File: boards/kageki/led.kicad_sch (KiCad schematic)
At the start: 50 parts

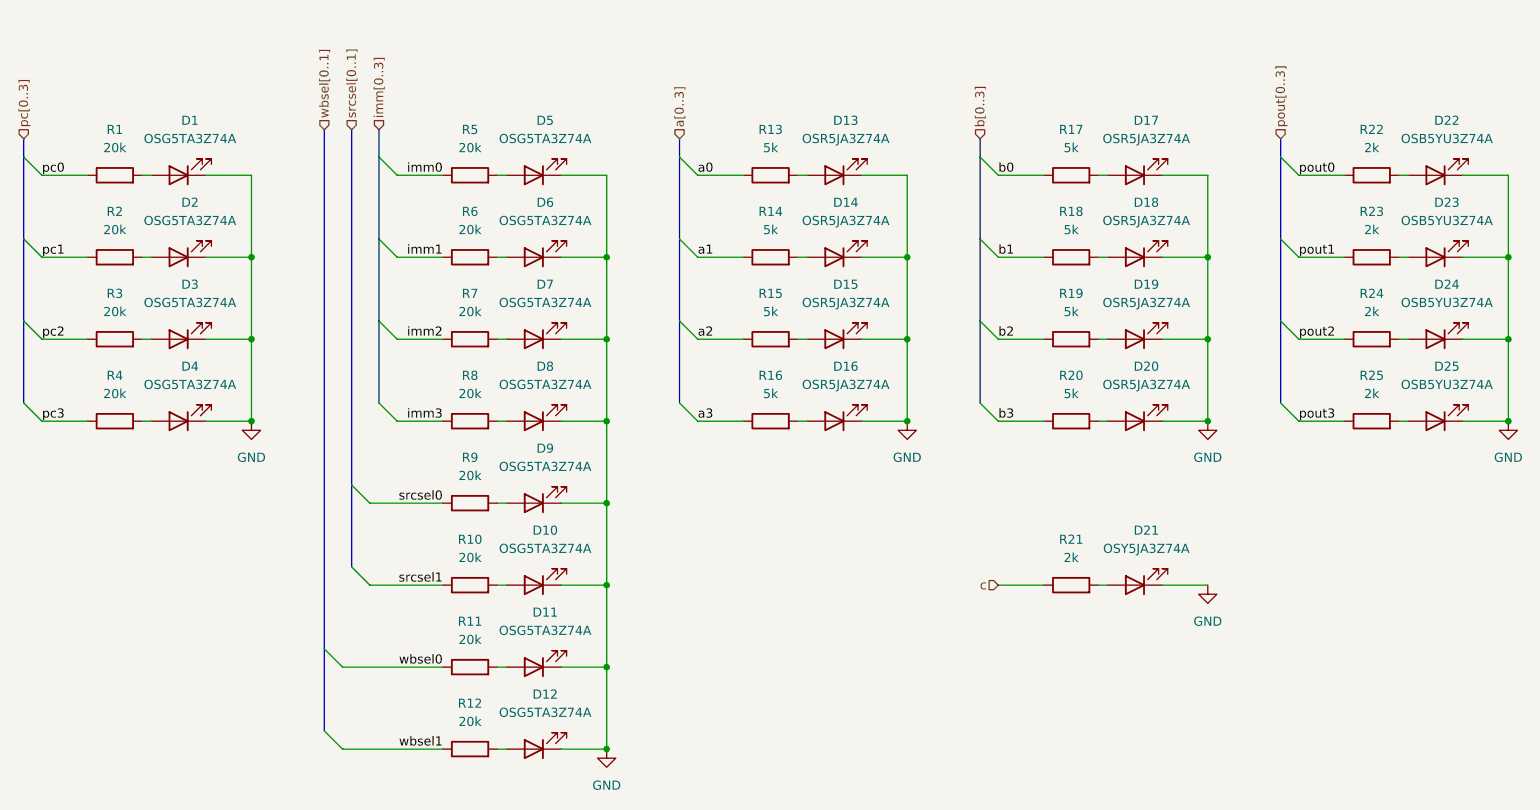
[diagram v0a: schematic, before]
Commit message: change values according to actual parts
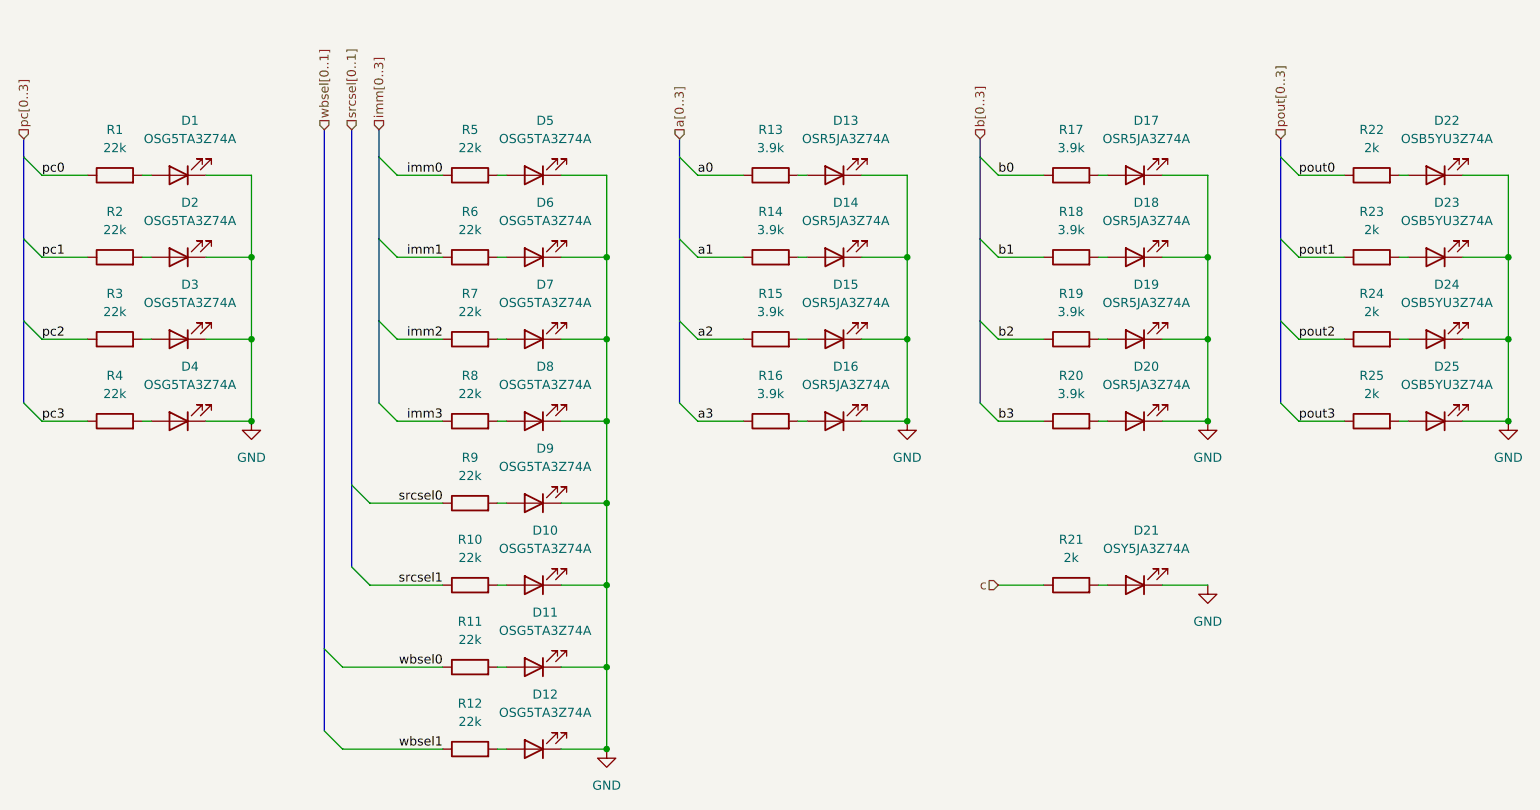
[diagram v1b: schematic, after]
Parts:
- R1, R10, R11, R12, R2, R3, R4, R5, R6, R7, R8, R9: value 20k -> 22k
- R13, R14, R15, R16, R17, R18, R19, R20: value 5k -> 3.9k
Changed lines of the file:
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@@
     (in_bom yes) (on_board yes) (fields_autoplaced)
     (property "Reference" "R6" (id 0) (at 88.9 43.18 90))
-    (property "Value" "20k" (id 1) (at 88.9 45.72 90))
+    (property "Value" "22k" (id 1) (at 88.9 45.72 90))
     (property "Footprint" "Resistor_SMD:R_0805_2012Metric_Pad1.20x1.40mm_HandSolder" (id 2) (at 88.9 51.308 90)
       (effects (font (size 1.27 1.27)) hide)
@@
     (in_bom yes) (on_board yes) (fields_autoplaced)
     (property "Reference" "R1" (id 0) (at 39.37 31.75 90))
-    (property "Value" "20k" (id 1) (at 39.37 34.29 90))
+    (property "Value" "22k" (id 1) (at 39.37 34.29 90))
     (property "Footprint" "Resistor_SMD:R_0805_2012Metric_Pad1.20x1.40mm_HandSolder" (id 2) (at 39.37 39.878 90)
       (effects (font (size 1.27 1.27)) hide)
@@
     (in_bom yes) (on_board yes) (fields_autoplaced)
     (property "Reference" "R10" (id 0) (at 88.9 88.9 90))
-    (property "Value" "20k" (id 1) (at 88.9 91.44 90))
+    (property "Value" "22k" (id 1) (at 88.9 91.44 90))
     (property "Footprint" "Resistor_SMD:R_0805_2012Metric_Pad1.20x1.40mm_HandSolder" (id 2) (at 88.9 97.028 90)
       (effects (font (size 1.27 1.27)) hide)
@@
     (in_bom yes) (on_board yes) (fields_autoplaced)
     (property "Reference" "R17" (id 0) (at 172.72 31.75 90))
-    (property "Value" "5k" (id 1) (at 172.72 34.29 90))
+    (property "Value" "3.9k" (id 1) (at 172.72 34.29 90))
     (property "Footprint" "Resistor_SMD:R_0805_2012Metric_Pad1.20x1.40mm_HandSolder" (id 2) (at 172.72 39.878 90)
       (effects (font (size 1.27 1.27)) hide)
@@
     (in_bom yes) (on_board yes) (fields_autoplaced)
     (property "Reference" "R9" (id 0) (at 88.9 77.47 90))
-    (property "Value" "20k" (id 1) (at 88.9 80.01 90))
+    (property "Value" "22k" (id 1) (at 88.9 80.01 90))
     (property "Footprint" "Resistor_SMD:R_0805_2012Metric_Pad1.20x1.40mm_HandSolder" (id 2) (at 88.9 85.598 90)
       (effects (font (size 1.27 1.27)) hide)
@@
     (in_bom yes) (on_board yes) (fields_autoplaced)
     (property "Reference" "R5" (id 0) (at 88.9 31.75 90))
-    (property "Value" "20k" (id 1) (at 88.9 34.29 90))
+    (property "Value" "22k" (id 1) (at 88.9 34.29 90))
     (property "Footprint" "Resistor_SMD:R_0805_2012Metric_Pad1.20x1.40mm_HandSolder" (id 2) (at 88.9 39.878 90)
       (effects (font (size 1.27 1.27)) hide)
@@
     (in_bom yes) (on_board yes) (fields_autoplaced)
     (property "Reference" "R7" (id 0) (at 88.9 54.61 90))
-    (property "Value" "20k" (id 1) (at 88.9 57.15 90))
+    (property "Value" "22k" (id 1) (at 88.9 57.15 90))
     (property "Footprint" "Resistor_SMD:R_0805_2012Metric_Pad1.20x1.40mm_HandSolder" (id 2) (at 88.9 62.738 90)
       (effects (font (size 1.27 1.27)) hide)
@@
     (in_bom yes) (on_board yes) (fields_autoplaced)
     (property "Reference" "R2" (id 0) (at 39.37 43.18 90))
-    (property "Value" "20k" (id 1) (at 39.37 45.72 90))
+    (property "Value" "22k" (id 1) (at 39.37 45.72 90))
     (property "Footprint" "Resistor_SMD:R_0805_2012Metric_Pad1.20x1.40mm_HandSolder" (id 2) (at 39.37 51.308 90)
       (effects (font (size 1.27 1.27)) hide)
@@
     (in_bom yes) (on_board yes) (fields_autoplaced)
     (property "Reference" "R13" (id 0) (at 130.81 31.75 90))
-    (property "Value" "5k" (id 1) (at 130.81 34.29 90))
+    (property "Value" "3.9k" (id 1) (at 130.81 34.29 90))
     (property "Footprint" "Resistor_SMD:R_0805_2012Metric_Pad1.20x1.40mm_HandSolder" (id 2) (at 130.81 39.878 90)
       (effects (font (size 1.27 1.27)) hide)
@@
     (in_bom yes) (on_board yes) (fields_autoplaced)
     (property "Reference" "R11" (id 0) (at 88.9 100.33 90))
-    (property "Value" "20k" (id 1) (at 88.9 102.87 90))
+    (property "Value" "22k" (id 1) (at 88.9 102.87 90))
     (property "Footprint" "Resistor_SMD:R_0805_2012Metric_Pad1.20x1.40mm_HandSolder" (id 2) (at 88.9 108.458 90)
       (effects (font (size 1.27 1.27)) hide)
@@
     (in_bom yes) (on_board yes) (fields_autoplaced)
     (property "Reference" "R15" (id 0) (at 130.81 54.61 90))
-    (property "Value" "5k" (id 1) (at 130.81 57.15 90))
+    (property "Value" "3.9k" (id 1) (at 130.81 57.15 90))
     (property "Footprint" "Resistor_SMD:R_0805_2012Metric_Pad1.20x1.40mm_HandSolder" (id 2) (at 130.81 62.738 90)
       (effects (font (size 1.27 1.27)) hide)
@@
     (in_bom yes) (on_board yes) (fields_autoplaced)
     (property "Reference" "R19" (id 0) (at 172.72 54.61 90))
-    (property "Value" "5k" (id 1) (at 172.72 57.15 90))
+    (property "Value" "3.9k" (id 1) (at 172.72 57.15 90))
     (property "Footprint" "Resistor_SMD:R_0805_2012Metric_Pad1.20x1.40mm_HandSolder" (id 2) (at 172.72 62.738 90)
       (effects (font (size 1.27 1.27)) hide)
@@
     (in_bom yes) (on_board yes) (fields_autoplaced)
     (property "Reference" "R14" (id 0) (at 130.81 43.18 90))
-    (property "Value" "5k" (id 1) (at 130.81 45.72 90))
+    (property "Value" "3.9k" (id 1) (at 130.81 45.72 90))
     (property "Footprint" "Resistor_SMD:R_0805_2012Metric_Pad1.20x1.40mm_HandSolder" (id 2) (at 130.81 51.308 90)
       (effects (font (size 1.27 1.27)) hide)
@@
     (in_bom yes) (on_board yes) (fields_autoplaced)
     (property "Reference" "R12" (id 0) (at 88.9 111.76 90))
-    (property "Value" "20k" (id 1) (at 88.9 114.3 90))
+    (property "Value" "22k" (id 1) (at 88.9 114.3 90))
     (property "Footprint" "Resistor_SMD:R_0805_2012Metric_Pad1.20x1.40mm_HandSolder" (id 2) (at 88.9 119.888 90)
       (effects (font (size 1.27 1.27)) hide)
@@
     (in_bom yes) (on_board yes) (fields_autoplaced)
     (property "Reference" "R8" (id 0) (at 88.9 66.04 90))
-    (property "Value" "20k" (id 1) (at 88.9 68.58 90))
+    (property "Value" "22k" (id 1) (at 88.9 68.58 90))
     (property "Footprint" "Resistor_SMD:R_0805_2012Metric_Pad1.20x1.40mm_HandSolder" (id 2) (at 88.9 74.168 90)
       (effects (font (size 1.27 1.27)) hide)
@@
     (in_bom yes) (on_board yes) (fields_autoplaced)
     (property "Reference" "R18" (id 0) (at 172.72 43.18 90))
-    (property "Value" "5k" (id 1) (at 172.72 45.72 90))
+    (property "Value" "3.9k" (id 1) (at 172.72 45.72 90))
     (property "Footprint" "Resistor_SMD:R_0805_2012Metric_Pad1.20x1.40mm_HandSolder" (id 2) (at 172.72 51.308 90)
       (effects (font (size 1.27 1.27)) hide)
@@
     (in_bom yes) (on_board yes) (fields_autoplaced)
     (property "Reference" "R4" (id 0) (at 39.37 66.04 90))
-    (property "Value" "20k" (id 1) (at 39.37 68.58 90))
+    (property "Value" "22k" (id 1) (at 39.37 68.58 90))
     (property "Footprint" "Resistor_SMD:R_0805_2012Metric_Pad1.20x1.40mm_HandSolder" (id 2) (at 39.37 74.168 90)
       (effects (font (size 1.27 1.27)) hide)
@@
     (in_bom yes) (on_board yes) (fields_autoplaced)
     (property "Reference" "R16" (id 0) (at 130.81 66.04 90))
-    (property "Value" "5k" (id 1) (at 130.81 68.58 90))
+    (property "Value" "3.9k" (id 1) (at 130.81 68.58 90))
     (property "Footprint" "Resistor_SMD:R_0805_2012Metric_Pad1.20x1.40mm_HandSolder" (id 2) (at 130.81 74.168 90)
       (effects (font (size 1.27 1.27)) hide)
@@
     (in_bom yes) (on_board yes) (fields_autoplaced)
     (property "Reference" "R20" (id 0) (at 172.72 66.04 90))
-    (property "Value" "5k" (id 1) (at 172.72 68.58 90))
+    (property "Value" "3.9k" (id 1) (at 172.72 68.58 90))
     (property "Footprint" "Resistor_SMD:R_0805_2012Metric_Pad1.20x1.40mm_HandSolder" (id 2) (at 172.72 74.168 90)
       (effects (font (size 1.27 1.27)) hide)
@@
     (in_bom yes) (on_board yes) (fields_autoplaced)
     (property "Reference" "R3" (id 0) (at 39.37 54.61 90))
-    (property "Value" "20k" (id 1) (at 39.37 57.15 90))
+    (property "Value" "22k" (id 1) (at 39.37 57.15 90))
     (property "Footprint" "Resistor_SMD:R_0805_2012Metric_Pad1.20x1.40mm_HandSolder" (id 2) (at 39.37 62.738 90)
       (effects (font (size 1.27 1.27)) hide)
